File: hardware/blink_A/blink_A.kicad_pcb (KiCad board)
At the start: 2 copper layers, 119 x 92 mm, 164 parts, among them J1 Conn_01x02, J11 KH-BNC50-3511, J12 KH-BNC50-3511, J13 KH-BNC50-3511, J14 Conn_02x16_Odd_Even, J15 Conn_01x01, J16 Conn_01x01, J2 PJ-320D, J3 PJ-320D, J4 KH-BNC50-3511, J5 Conn_01x06_Pin, J6 Conn_01x03, J7 Conn_01x06_Pin, J9 USB_C_Receptacle, Q3 2N7002, Q4 2N7002, Q5 2N7002, SW1 SW_SPDT, SW2 SW_Push_4PDT, SW3 SW_Push_4PDT, SW4 SW_Push_4PDT, U1 AMS1117-3.3, U10 TMP112AIDRLR, U11 MAX40200AUK, U12 MAX40200AUK, U13 AMS1117-3.3, U14 SN74LVC1G14DBV, U16 TPS63060, U2 AD8397, U3 M24C02-RMN, U4 STM32F405RGTx, U5 SN74LVC1G14DBV, U6 SN74LVC1G14DBV, U7 CH340C, U8 USBLC6-2P6, U9 MCP73832-2-OT, X1 GTXO-14V (2.048MHz), Y1 16MHz

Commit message: typo
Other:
- board text added: "Blink Rev A Cullen Jennings 2024"
- board text removed: "Blink RevA Cullen Jennings 2024"
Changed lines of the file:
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@@
 		(layer "Edge.Cuts")
 	)
-	(gr_text "Blink RevA Cullen Jennings 2024"
+	(gr_text "Blink Rev A Cullen Jennings 2024"
 		(at 175.22069 41.354948 0)
 		(layer "F.SilkS")

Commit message: updates
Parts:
- X1: footprint Oscillator:Oscillator_DIP-14 -> blinky_footprints:OSC_DIP-14
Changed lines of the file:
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@@
 		)
 	)
-	(footprint "Oscillator:Oscillator_DIP-14"
+	(footprint "blinky_footprints:OSC_DIP-14"
 		(layer "F.Cu")
 		(at 130.88 105.11)
@@
 			(at 7.62 -11.26 0)
 			(layer "F.SilkS")
+			(hide yes)
 			(effects
 				(font
@@
 			)
 		)
-		(property "Footprint" "Oscillator:Oscillator_DIP-14"
+		(property "Footprint" "blinky_footprints:OSC_DIP-14"
 			(at 0 0 0)
 			(unlocked yes)
@@
 			(layer "F.SilkS")
 		)
+		(fp_circle
+			(center -1.7 1.5)
+			(end -1.2 1.5)
+			(stroke
+				(width 0.2)
+				(type solid)
+			)
+			(fill solid)
+			(layer "F.SilkS")
+		)
 		(fp_line
 			(start -2.98 -10.41)
@@
 				)
 			)
+		)
+		(pad "" np_thru_hole rect
+			(at -1.53 -3.81)
+			(size 2 4)
+			(drill 1.5)
+			(layers "F&B.Cu" "*.Mask")
+		)
+		(pad "" np_thru_hole rect
+			(at 16.77 -3.81)
+			(size 2 4)
+			(drill 1.5)
+			(layers "F&B.Cu" "*.Mask")
 		)
 		(pad "1" thru_hole rect
@@
 			(pintype "power_in")
 		)
-		(model "${KICAD8_3DMODEL_DIR}/Oscillator.3dshapes/Oscillator_DIP-14.wrl"
+		(model "${KICAD6_3DMODEL_DIR}/Oscillator.3dshapes/Oscillator_DIP-14.wrl"
 			(offset
 				(xyz 0 0 0)

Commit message: update version
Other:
- board text added: "Blink Rev A.2 Cullen Jennings 2024"
- board text removed: "Blink Rev A Cullen Jennings 2024"
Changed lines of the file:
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@@
 	(title_block
 		(title "Blink")
-		(date "2024-05-14")
-		(rev "A")
+		(date "2024-05-27")
+		(rev "A.2")
 		(company "Cullen Jennings")
 	)
@@
 		(layer "Edge.Cuts")
 	)
-	(gr_text "Blink Rev A Cullen Jennings 2024"
+	(gr_text "Blink Rev A.2 Cullen Jennings 2024"
 		(at 175.22069 41.354948 0)
 		(layer "F.SilkS")

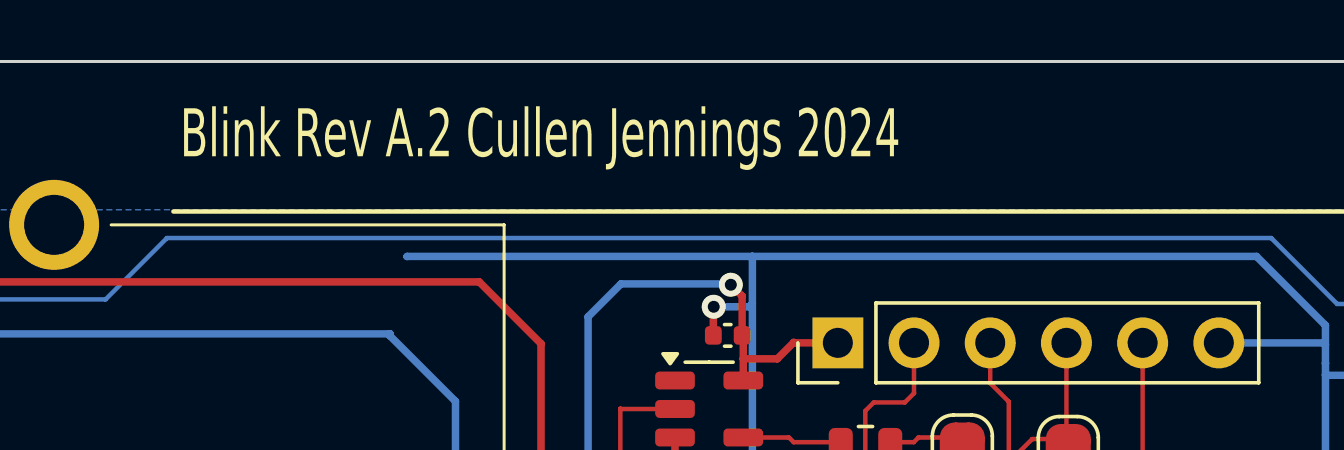
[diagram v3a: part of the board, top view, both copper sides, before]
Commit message: moving blink to V A.1
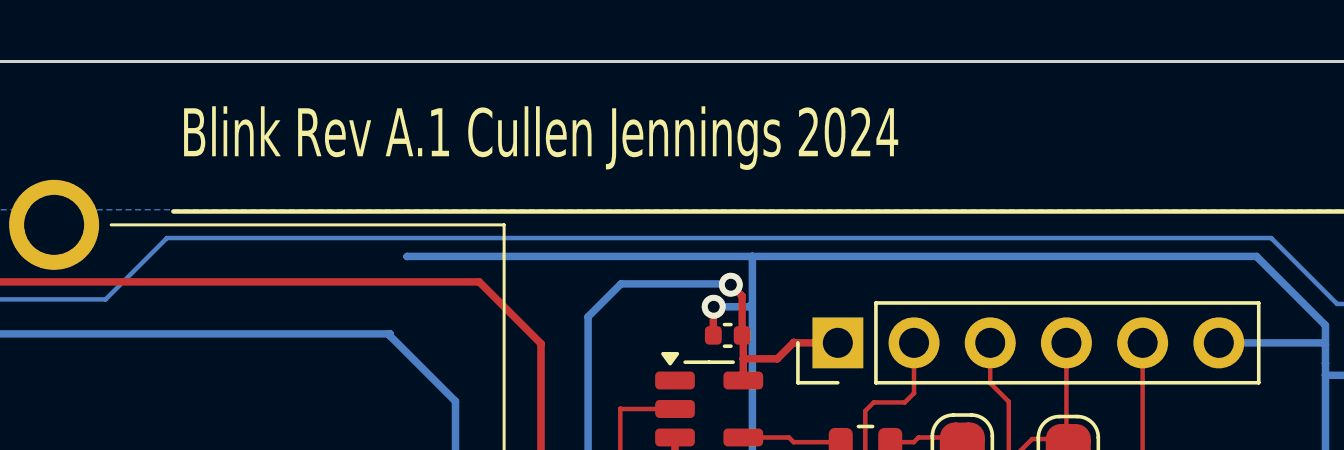
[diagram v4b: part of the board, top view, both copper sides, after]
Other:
- board text added: "Blink Rev A.1 Cullen Jennings 2024"
- board text removed: "Blink Rev A.2 Cullen Jennings 2024"
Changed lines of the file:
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@@
 	(title_block
 		(title "Blink")
-		(date "2024-05-27")
-		(rev "A.2")
+		(date "2024-06-09")
+		(rev "A.1")
 		(company "Cullen Jennings")
 	)
@@
 		(layer "Edge.Cuts")
 	)
-	(gr_text "Blink Rev A.2 Cullen Jennings 2024"
+	(gr_text "Blink Rev A.1 Cullen Jennings 2024"
 		(at 175.22069 41.354948 0)
 		(layer "F.SilkS")
